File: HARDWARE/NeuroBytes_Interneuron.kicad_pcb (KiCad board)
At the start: 2 copper layers, 58.4 x 25 mm, 29 parts, among them P1 CONN_01X04, P12 CONN_01X07, P2 CONN_01X04, P3 CONN_01X04, P4 CONN_01X04, P5 CONN_01X04, P6 CONN_01X04, P7 CONN_01X04, Q1 NPN_dual, Q2 NPN_dual, SW1 SW_PUSH, U1 STM32L011Gx, U2 LD3985G33R

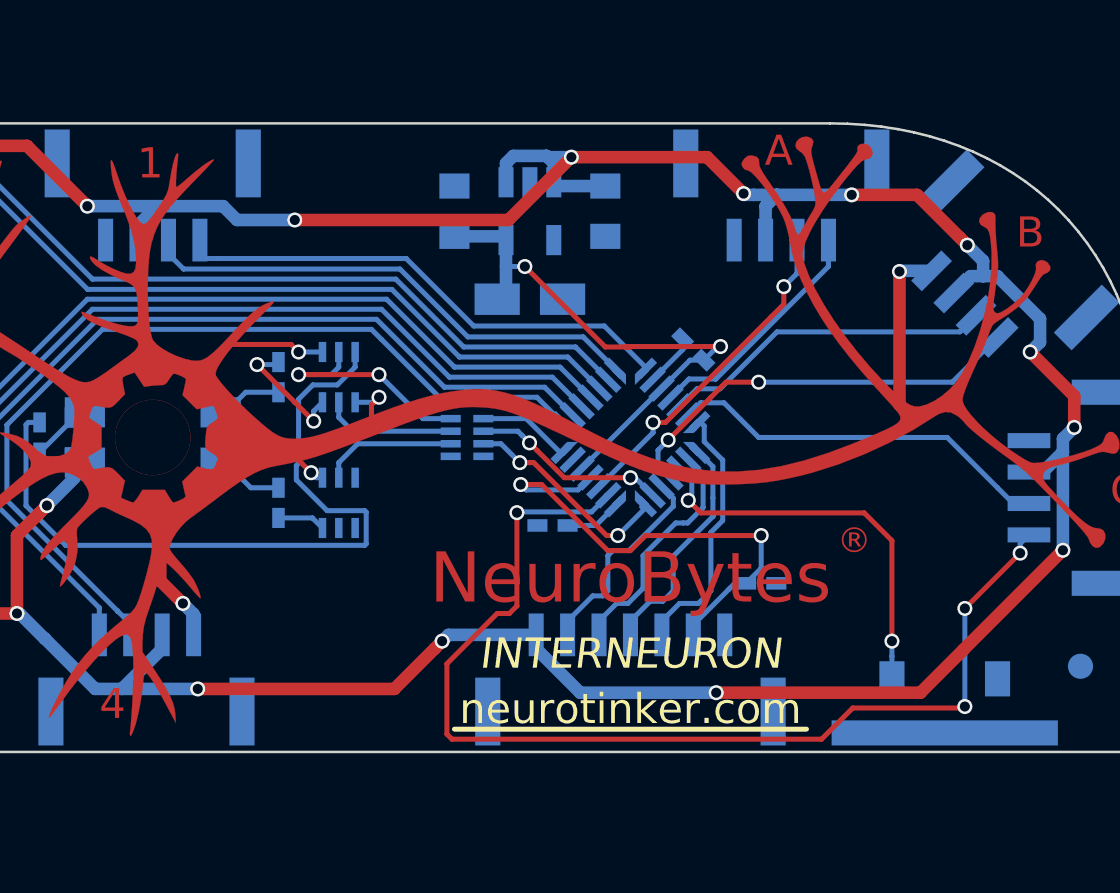
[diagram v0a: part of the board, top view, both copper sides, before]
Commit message: Added PCB mfr notes on FAB layer. Modified QFN28 footprint to comply with IPC-7351FC Level B.
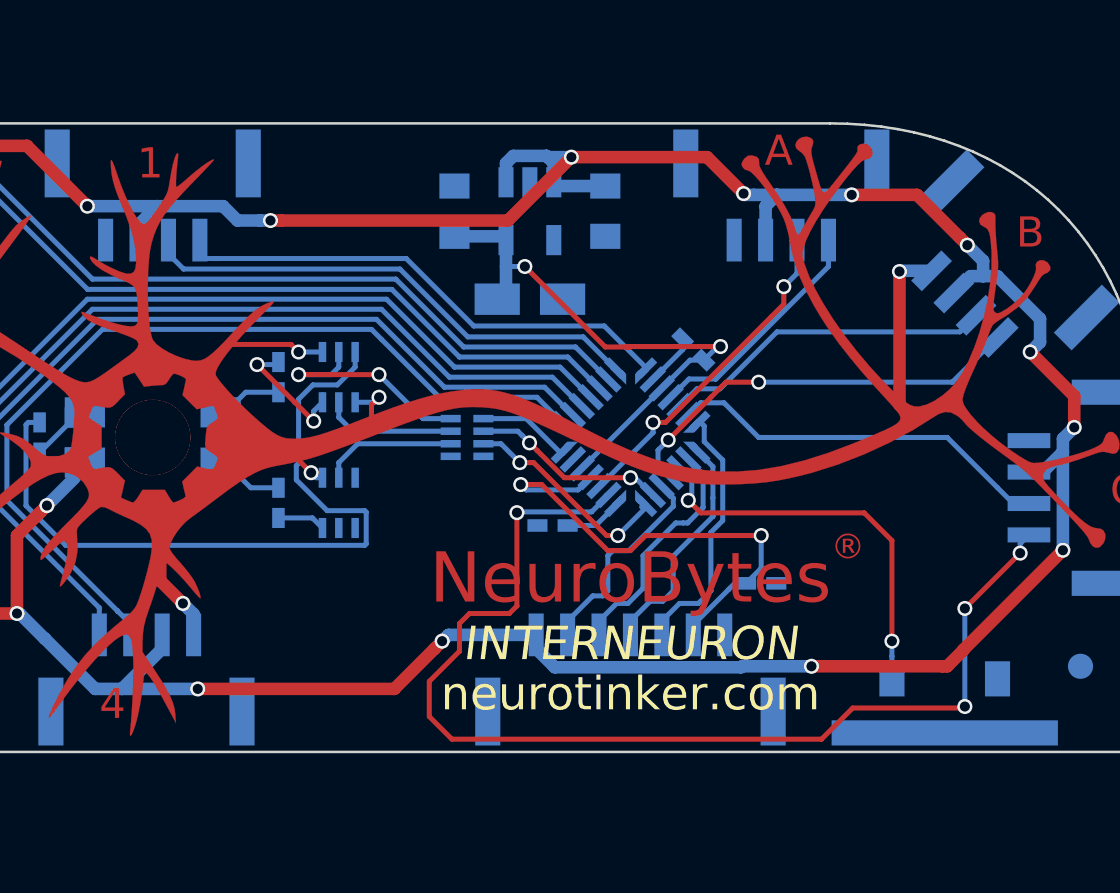
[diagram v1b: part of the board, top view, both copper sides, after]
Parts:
- removed the REF** at (157.5, 90.0)
- turned U1 to 135 degrees
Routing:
- net A3EX: track 43.9 -> 45.2 mm
- net +5V: track 153.8 -> 153.0 mm
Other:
- board text added: "COMPONENT POSITION ORIGIN"
- board text added: "NOTES: 1. FOOTPRINTS ORIENTED PER IPC-7351FC LEVEL B (PIN 1 IN LOWER LEFT) 2. COMPONENT ROTATION IN DEGREES COUNTER-CLOCKWISE 3. ALL COMPONENTS MOUNTED ON B.CU LAYER (LED IS BOTTOM-MOUNT) 4. PCB IS 1.6mm FR4 RATED FOR ROHS REFLOW, 1OZ COPPER, ENIG FINISH 5. MATTE BLACK SOLDER MASK WITH WHITE SILKSCREEN 6. SOLDER PASTE MUST BE ROHS COMPLIANT (LEAD-FREE) 7. NO MARKS (E-TEST, QA, SERIAL NUMBER, ETC)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"
- board text added: "ROUTE BOARD OUTLINE EXCEPT FOR TWO ENDS"
- board text added: "V-SCORE PARALLEL ENDS"

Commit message: Generated Gerber files, drill file, BOM, and placement file. Changed 7-pin JST connector designator to P8 (was P12, and P9-P11 don't exist).
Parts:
- removed P12: CONN_01X07, KiCad_Footprints:ZF_CONN_JST_GH_7POS
- added P8: JST GH 7-POS, KiCad_Footprints:ZF_CONN_JST_GH_7POS, B.Cu at (169.0, 100.2)
- C1, C4: value C -> 1u0
- C2: value CP -> 10u
- C3, C5: value C -> 0u1
- P1, P2, P3, P4, P5, P6, P7: value CONN_01X04 -> JST GH 4-POS
- R1: value R -> 150
- R2, R3: value R -> 100
- R4: value R -> JMP
- SW1: value SW_PUSH -> SW_PUSH_TL3330AF130QG
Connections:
- P1 pad : GND -> (no net)
- P2 pad : GND -> (no net)
- P3 pad : GND -> (no net)
- P4 pad : GND -> (no net)
- P5 pad : GND -> (no net)
- P6 pad : GND -> (no net)
- P7 pad : GND -> (no net)
- SW1 pad : GND -> (no net)
